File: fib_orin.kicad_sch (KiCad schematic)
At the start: 22 parts, among them IC5 TXB0108RGYR, IC6 TXB0108RGYR, IC7 TXB0108RGYR, IC9 TXB0108RGYR, J1201 Orin Nano

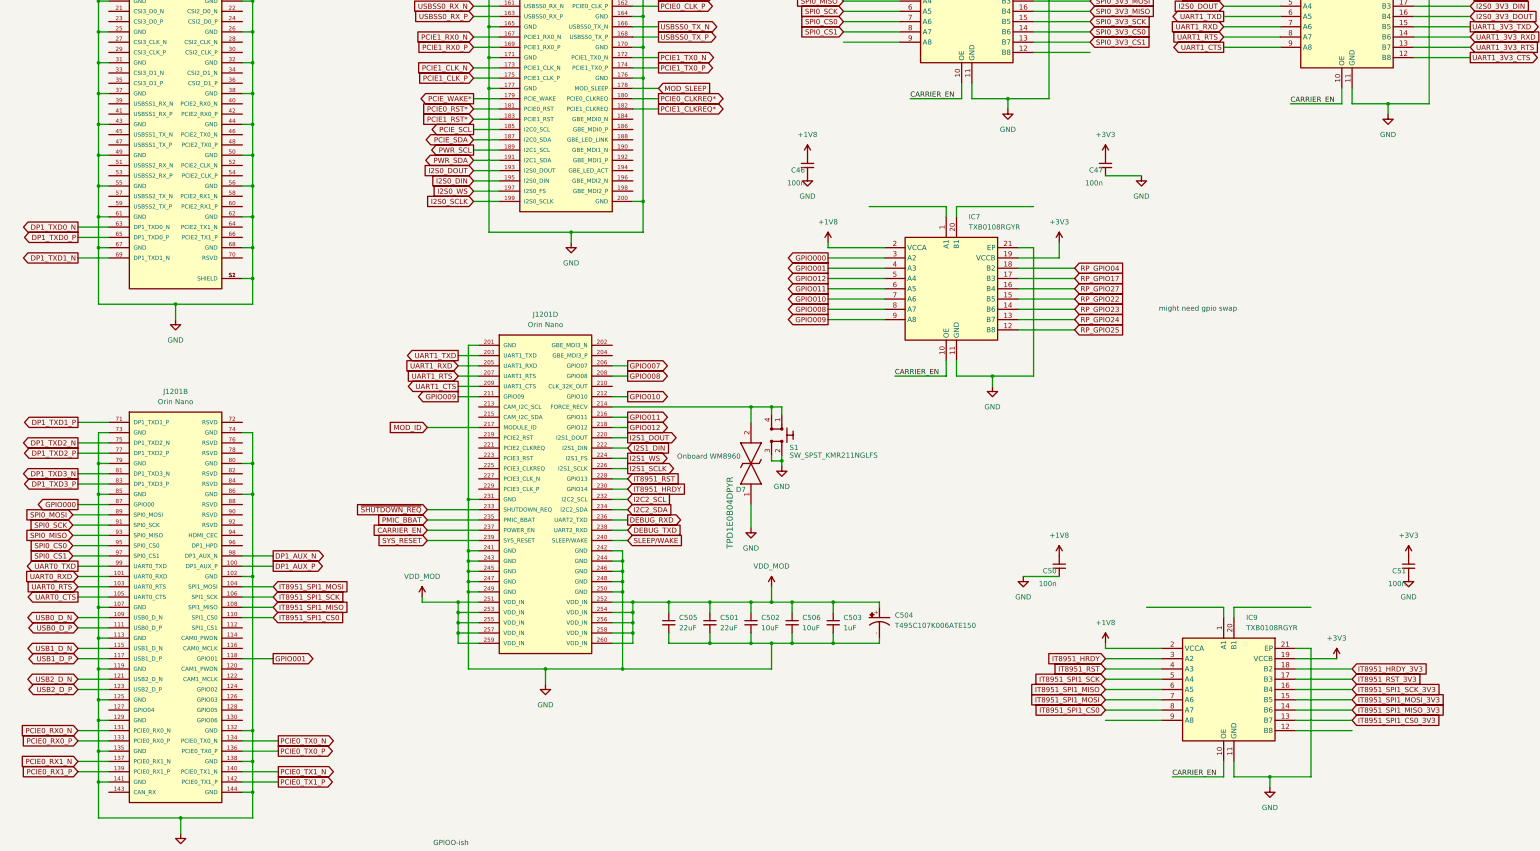
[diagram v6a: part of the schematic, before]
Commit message: routed epd displays, added testpoints and all the little checks and fixe, (regrettably) removed the i80 connector, 99% there, need to double check some things add peripheral connectors, shared-ish storage and vias vias vias
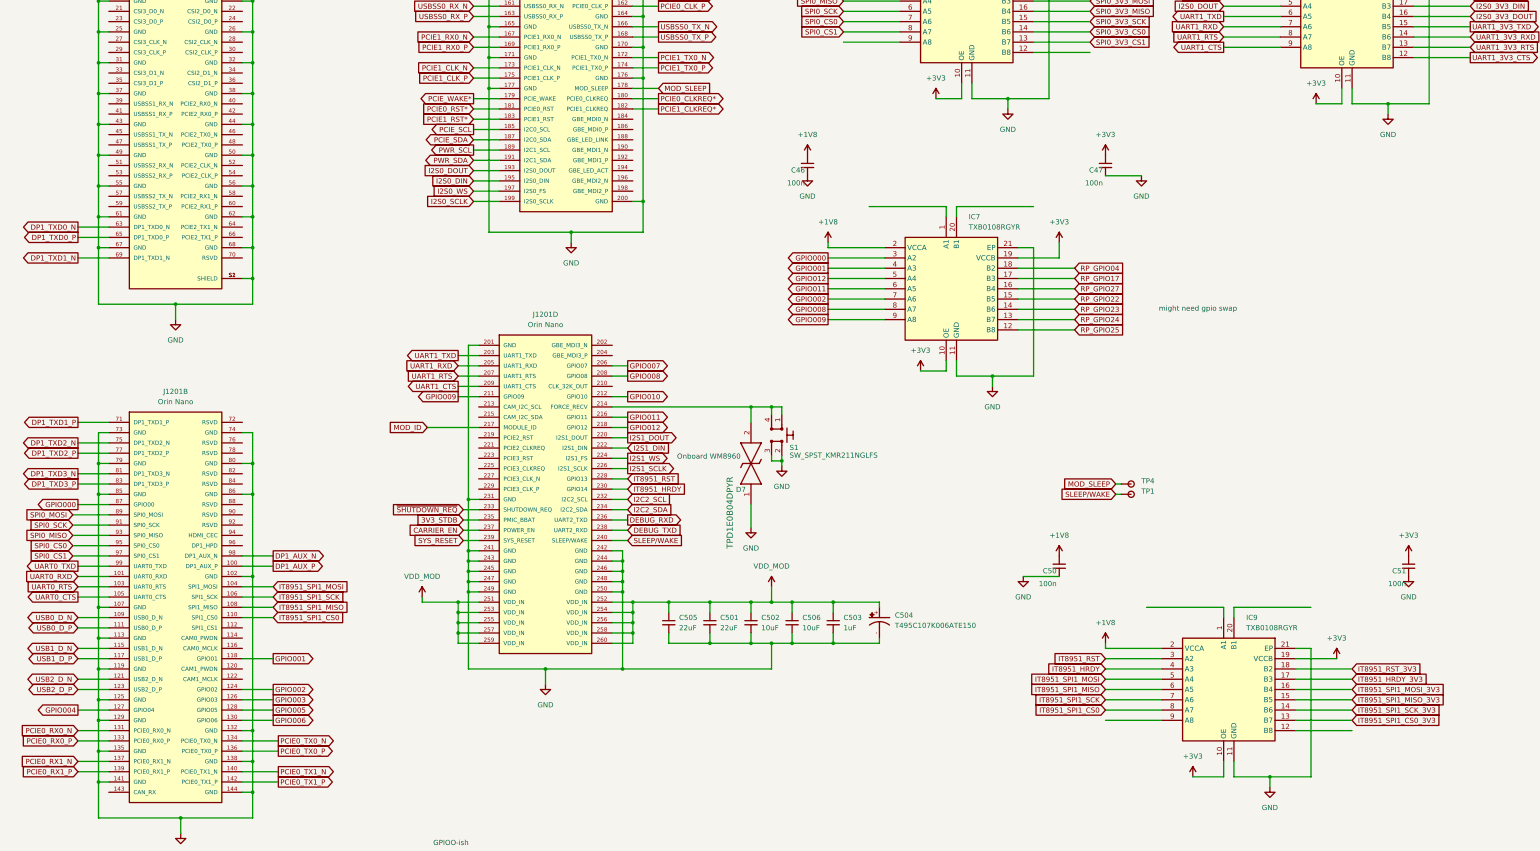
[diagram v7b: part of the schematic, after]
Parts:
- added TP1, TP4: TestPoint, TestPoint:TestPoint_Pad_D1.0mm, symbol Fibel2:TestPoint
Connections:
- net +3V3: now also IC5.10 (OE), IC6.10 (OE), IC7.10 (OE), IC9.10 (OE)
- net CARRIER_EN: no longer IC5.10 (OE), IC6.10 (OE), IC7.10 (OE), IC9.10 (OE)
- net GPIO010: no longer IC7.7 (A6)
- net IT8951_HRDY: now also IC9.4 (A3); no longer IC9.3 (A2)
- net IT8951_HRDY_3V3: now also IC9.17 (B3); no longer IC9.18 (B2)
- net IT8951_RST: now also IC9.3 (A2); no longer IC9.4 (A3)
- net IT8951_RST_3V3: now also IC9.18 (B2); no longer IC9.17 (B3)
- net IT8951_SPI1_MISO_3V3: now also IC9.15 (B5); no longer IC9.14 (B6)
- net IT8951_SPI1_MOSI: now also IC9.5 (A4); no longer IC9.7 (A6)
- net IT8951_SPI1_MOSI_3V3: now also IC9.16 (B4); no longer IC9.15 (B5)
- net IT8951_SPI1_SCK: now also IC9.7 (A6); no longer IC9.5 (A4)
- net IT8951_SPI1_SCK_3V3: now also IC9.14 (B6); no longer IC9.16 (B4)
- net MOD_SLEEP: now also TP4.1
- net SLEEP/WAKE: now also TP1.1
- net GPIO002: now reaches J1201.124 (GPIO02)
- net GPIO002: now also IC7.7 (A6)
- net GPIO003: now reaches J1201.126 (GPIO03)
- net GPIO004: now reaches J1201.127 (GPIO04)
- net GPIO005: now reaches J1201.128 (GPIO05)
- net GPIO006: now reaches J1201.130 (GPIO06)
- net PMIC_BBAT renamed 3V3_STDB

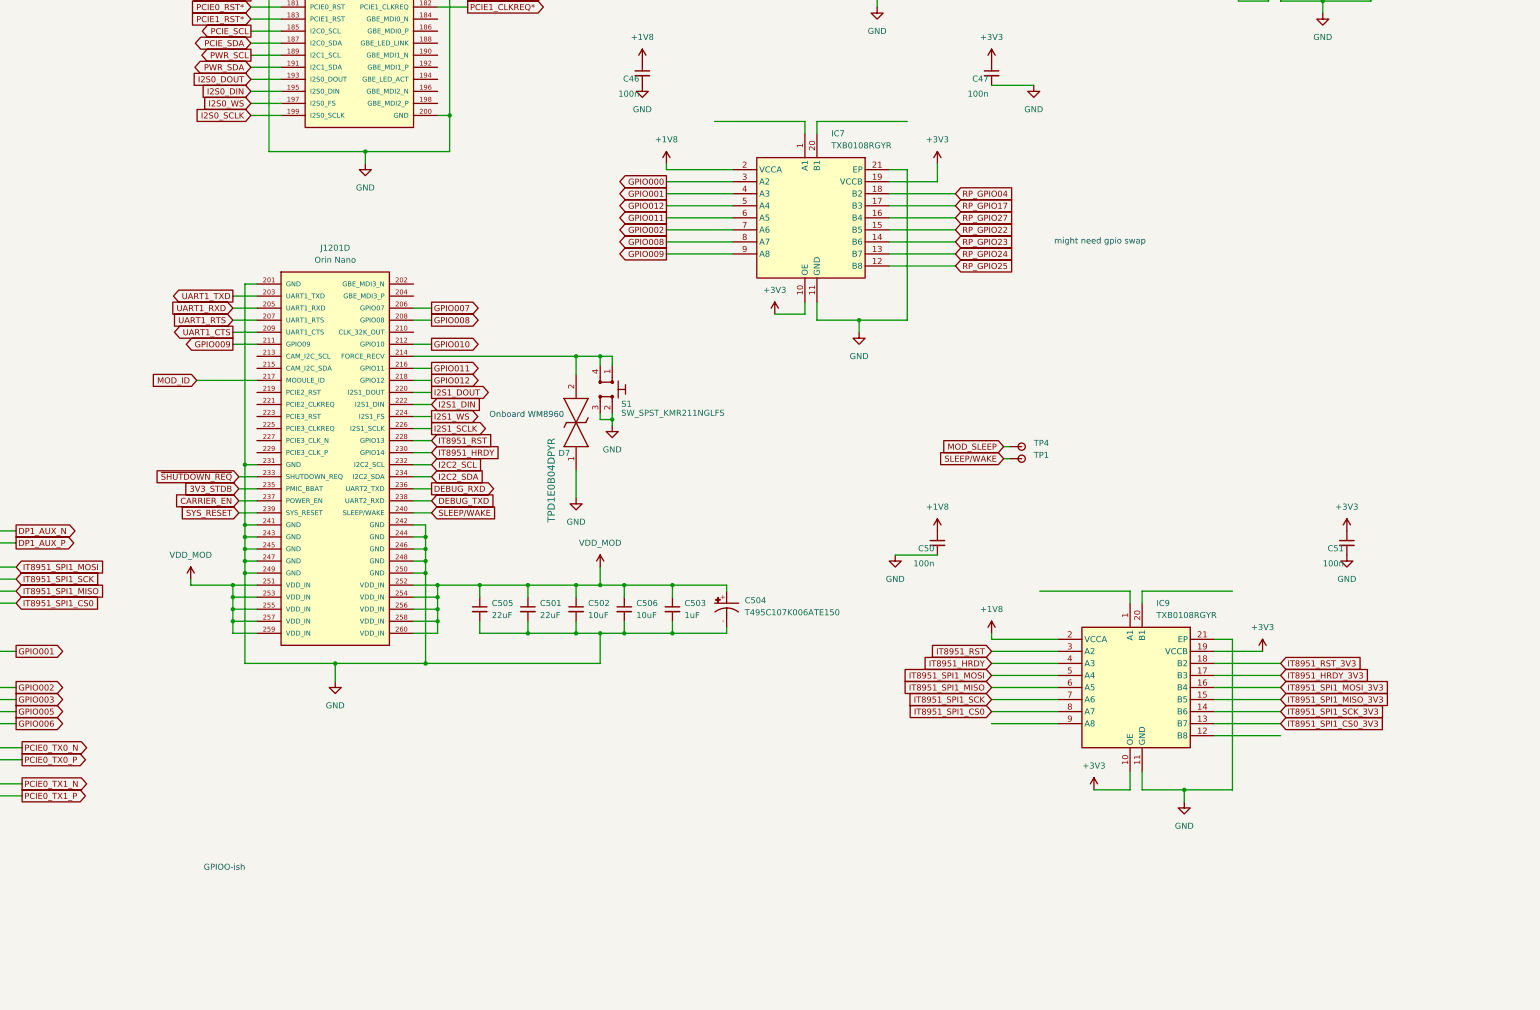
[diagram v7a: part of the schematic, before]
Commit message: finished routing, sanity check and prep fabrication files next
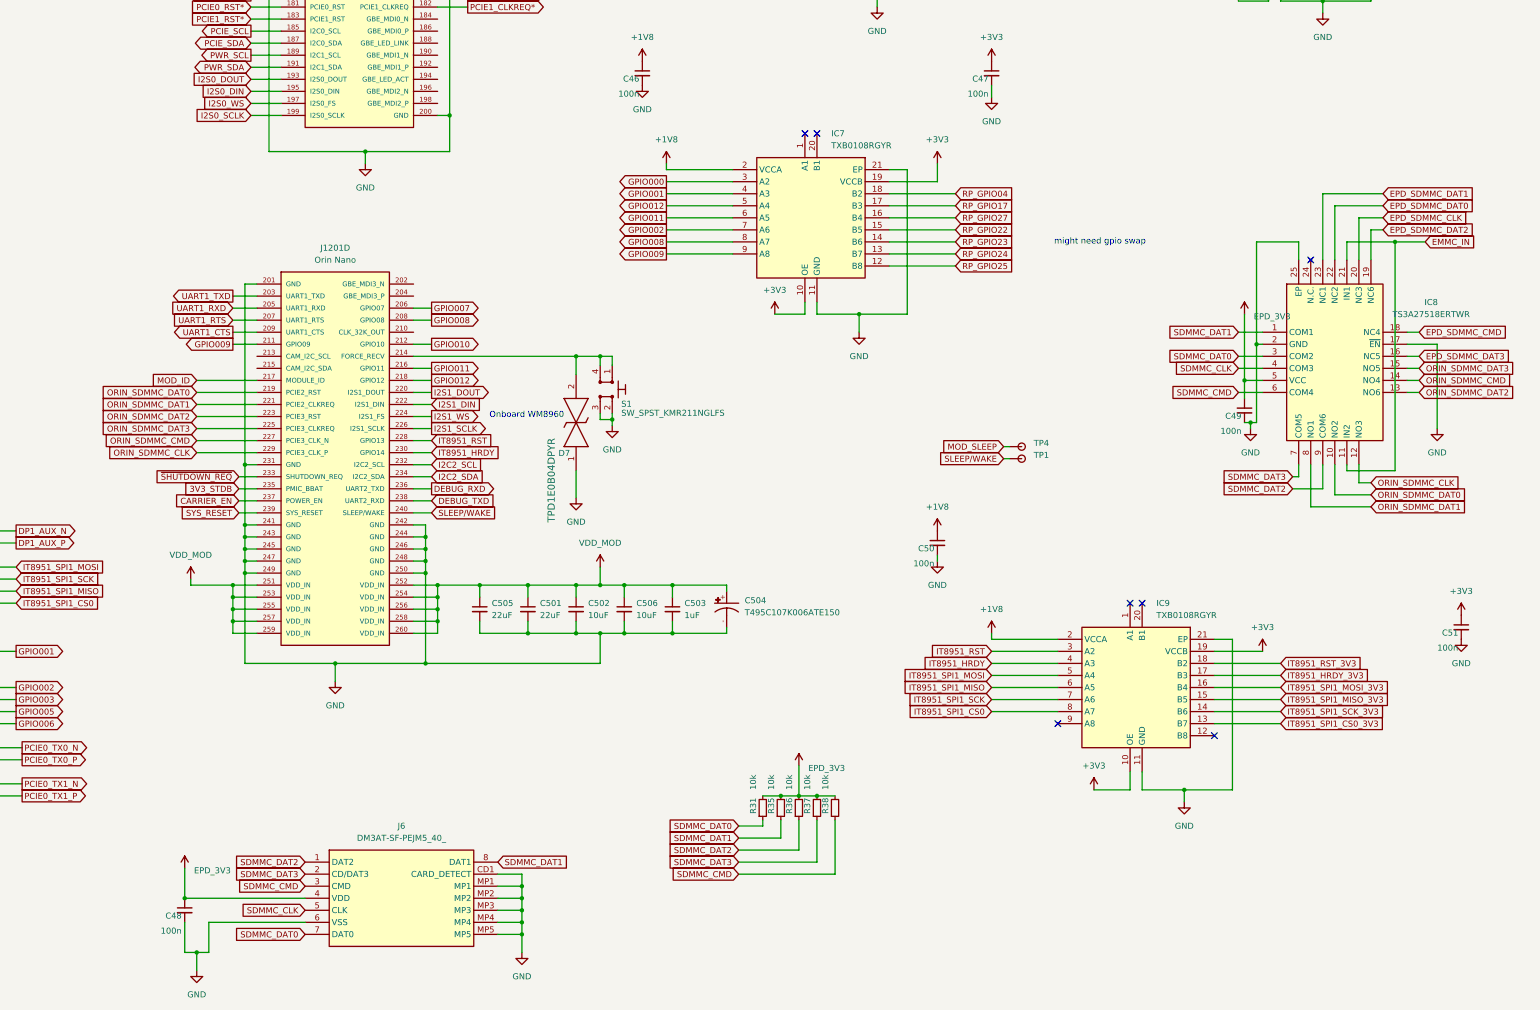
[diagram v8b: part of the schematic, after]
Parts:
- added C48, C49: 100nF, Capacitor_SMD:C_0402_1005Metric, symbol Fibel2:C_Small_Rota
- added IC8: TS3A27518ERTWR, Fibel2:QFN50P400X400X80-25N, symbol Fibel2:TS3A27518ERTWR
- added J6: DM3AT-SF-PEJM5_40_, Fibel2:DM3ATSFPEJM540, symbol Fibel2:DM3AT-SF-PEJM5_40_
- added R31, R35, R36, R37, R38: 10K, Resistor_SMD:R_0402_1005Metric, symbol Fibel2:R_Small_Rota
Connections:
- net GND: now also C48.2, C49.2, IC8.17 (~{EN}), IC8.2 (GND), IC8.25 (EP), J6.6 (VSS), J6.CD1 (CARD_DETECT), J6.MP1, J6.MP2, J6.MP3, J6.MP4, J6.MP5
- net ORIN_SDMMC_DAT0: now reaches J1201.219 (PCIE2_RST)
- net ORIN_SDMMC_DAT0: now also IC8.10 (NO2)
- net ORIN_SDMMC_DAT1: now reaches J1201.221 (PCIE2_CLKREQ)
- net ORIN_SDMMC_DAT1: now also IC8.8 (NO1)
- net ORIN_SDMMC_DAT2: now reaches J1201.223 (PCIE3_RST)
- net ORIN_SDMMC_DAT2: now also IC8.13 (NO6)
- net ORIN_SDMMC_DAT3: now reaches J1201.225 (PCIE3_CLKREQ)
- net ORIN_SDMMC_DAT3: now also IC8.15 (NO5)
- net ORIN_SDMMC_CMD: now reaches J1201.227 (PCIE3_CLK_N)
- net ORIN_SDMMC_CMD: now also IC8.14 (NO4)
- net ORIN_SDMMC_CLK: now reaches J1201.229 (PCIE3_CLK_P)
- net ORIN_SDMMC_CLK: now also IC8.12 (NO3)
- new net EMMC_IN: IC8.11 (IN2), IC8.21 (IN1)
- new net EPD_3V3: C48.1, C49.1, IC8.5 (VCC), J6.4 (VDD), R31.2, R35.2, R36.2, R37.2, R38.2
- new net EPD_SDMMC_CLK: IC8.20 (NC3)
- new net EPD_SDMMC_CMD: IC8.18 (NC4)
- new net EPD_SDMMC_DAT0: IC8.22 (NC2)
- new net EPD_SDMMC_DAT1: IC8.23 (NC1)
- new net EPD_SDMMC_DAT2: IC8.19 (NC6)
- new net EPD_SDMMC_DAT3: IC8.16 (NC5)
- new net SDMMC_CLK: IC8.4 (COM3), J6.5 (CLK)
- new net SDMMC_CMD: IC8.6 (COM4), J6.3 (CMD), R38.1
- new net SDMMC_DAT0: IC8.3 (COM2), J6.7 (DAT0), R31.1
- new net SDMMC_DAT1: IC8.1 (COM1), J6.8 (DAT1), R35.1
- new net SDMMC_DAT2: IC8.9 (COM6), J6.1 (DAT2), R36.1
- new net SDMMC_DAT3: IC8.7 (COM5), J6.2 (CD/DAT3), R37.1
- no-connect marks 0 -> 7
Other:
- note removed: "GPIOO-ish"
- moved on the sheet: C51
